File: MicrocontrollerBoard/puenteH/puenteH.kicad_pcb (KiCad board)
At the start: 2 copper layers, 78.7 x 63.5 mm, 54 parts, among them J1 PROG_CONN, J10 PCA_5V, J11 PCB_5V, J12 PDA_5V, J13 PA_GND, J14 PBA_GND, J15 PCA_GND, J16 PCB_GND, J17 PDA_GND, J18 COM, J19 COM_5V, J2 5V_CONN, J20 COM_GND, J21 POWER_CONN, J22 MOTOR2, J23 MOTOR1, J3 PA, J4 PBA, J5 PCA, J6 PCB, J7 PDA, J8 PA_5V, J9 PBA_5V, U1 ATmega1284P-PU, U2 TC4422, U3 TC4422, U4 TC4422, U5 TC4422, Y1 16MHz

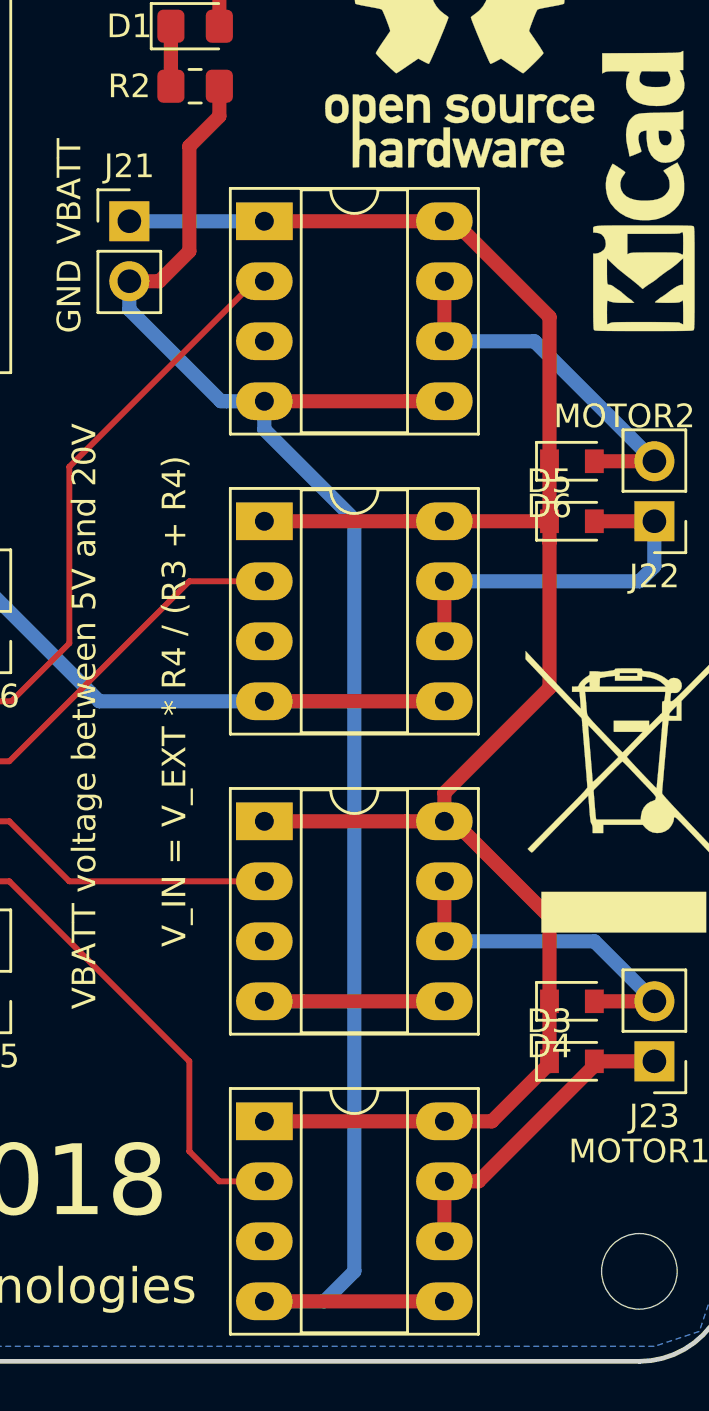
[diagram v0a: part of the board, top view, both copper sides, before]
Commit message: Changed TC4422 footprints to non socket so the 3D model has the chips.
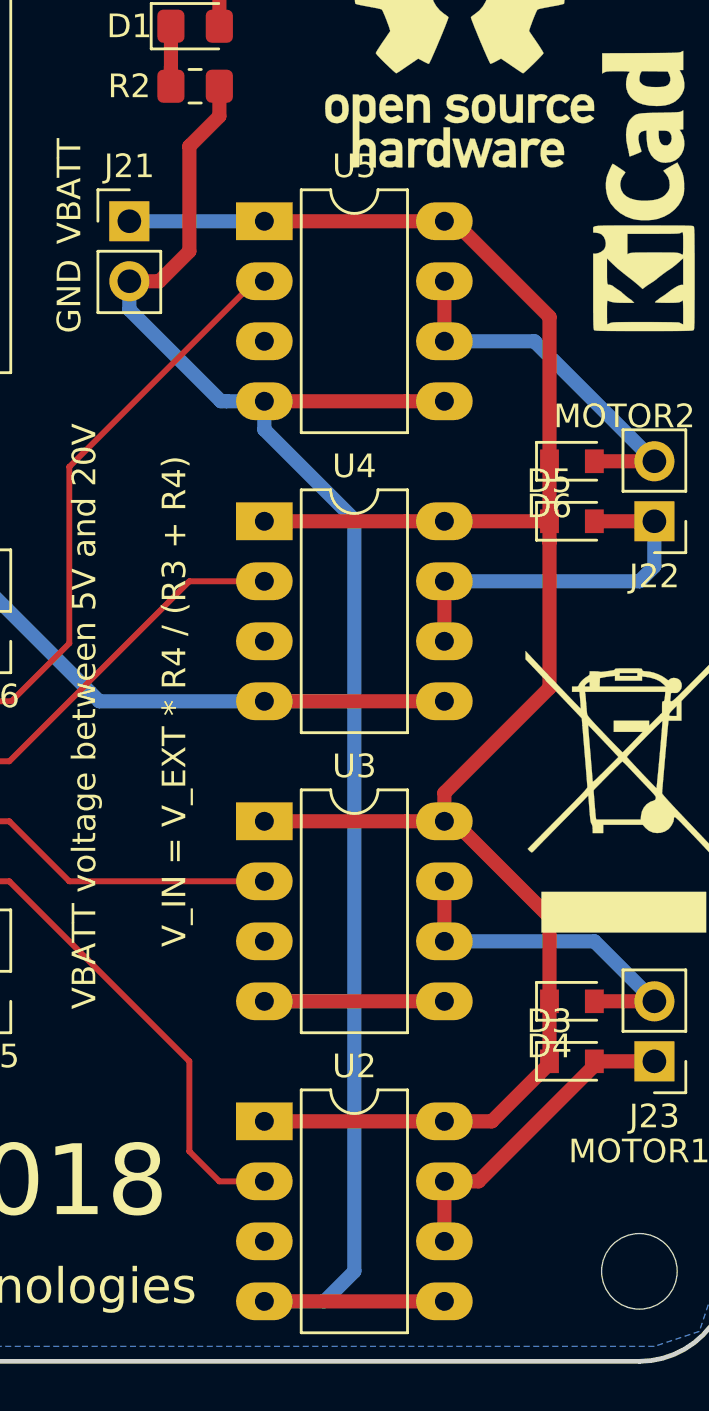
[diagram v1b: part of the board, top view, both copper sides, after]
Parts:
- U2, U3, U4, U5: footprint Package_DIP:DIP-8_W7.62mm_Socket_LongPads -> Package_DIP:DIP-8_W7.62mm_LongPads

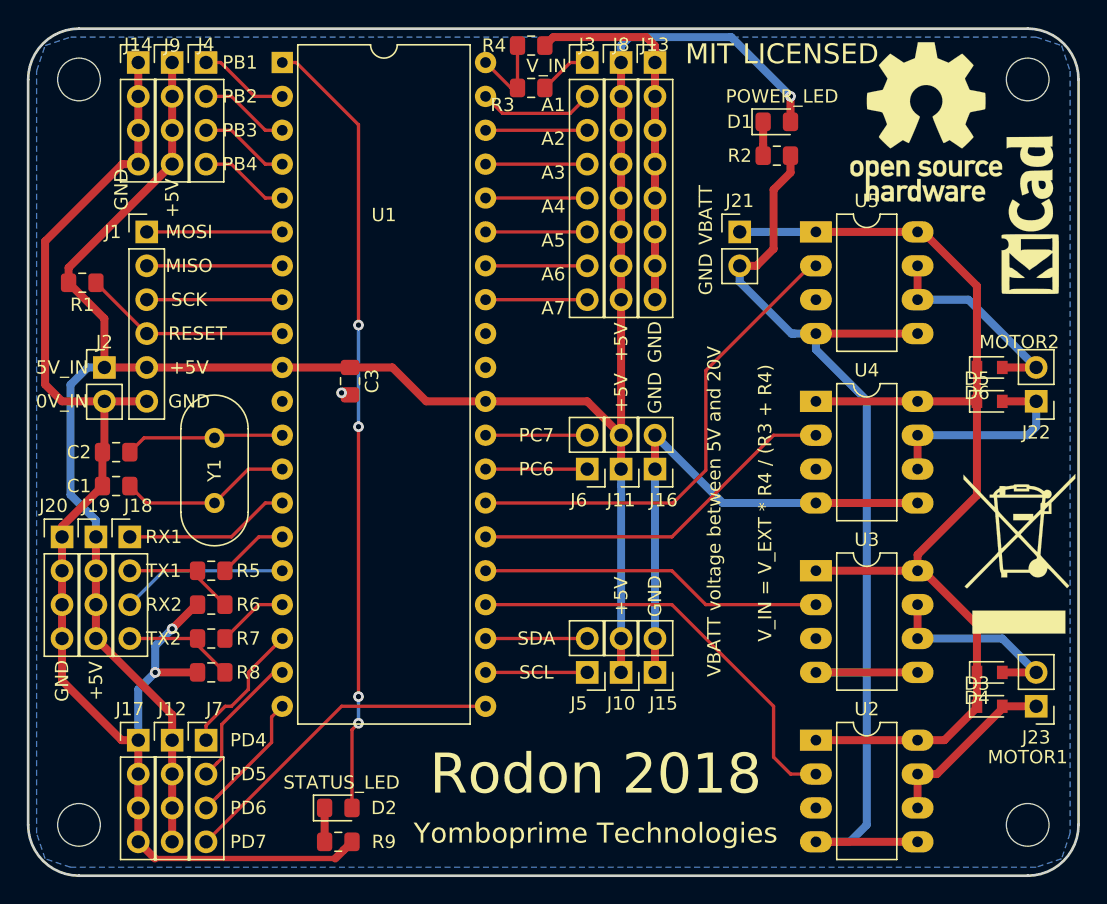
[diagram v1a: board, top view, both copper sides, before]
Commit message: Microcontroller bord: Fixed PWM lines not going to uc's PWM pins. Added 3V3 regulator.
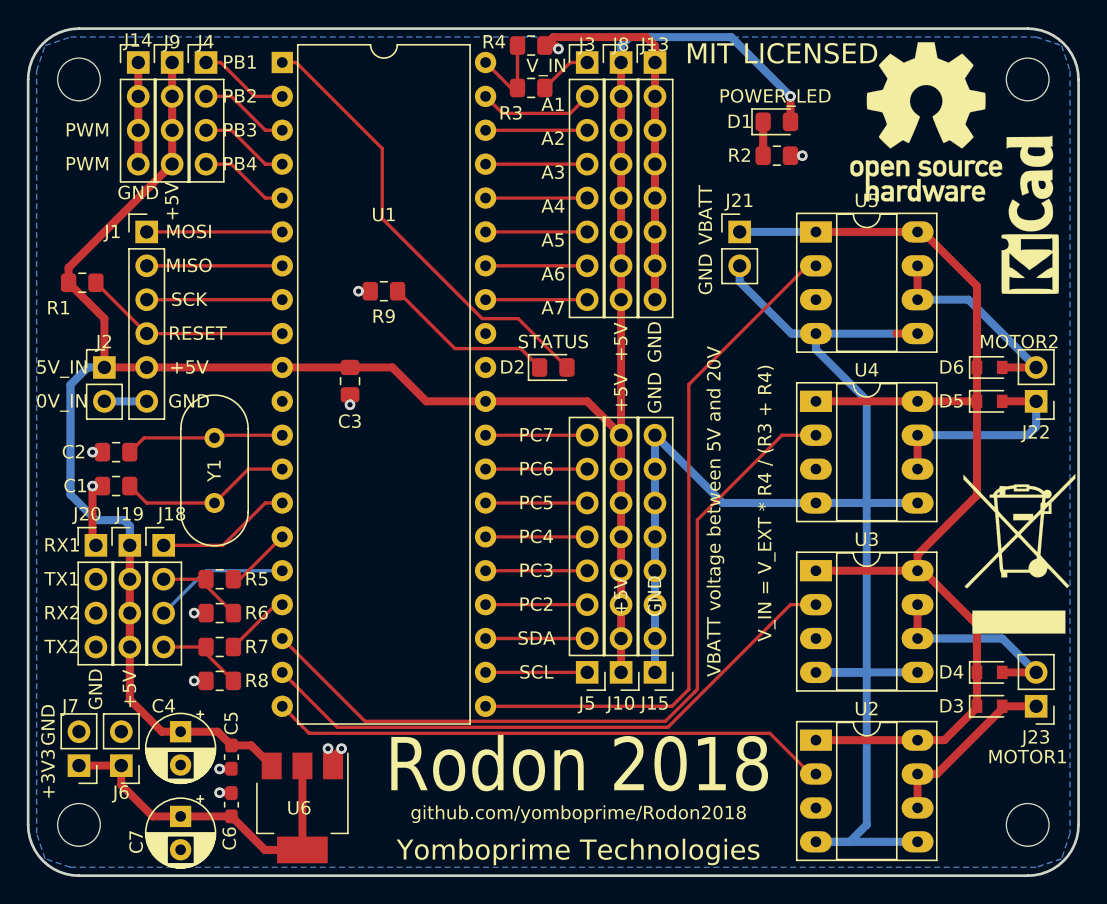
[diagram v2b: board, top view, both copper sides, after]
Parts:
- removed J11: PCB_5V, Connector_PinHeader_2.54mm:PinHeader_1x02_P2.54mm_Vertical
- removed J12: PDA_5V, Connector_PinHeader_2.54mm:PinHeader_1x04_P2.54mm_Vertical
- removed J16: PCB_GND, Connector_PinHeader_2.54mm:PinHeader_1x02_P2.54mm_Vertical
- removed J17: PDA_GND, Connector_PinHeader_2.54mm:PinHeader_1x04_P2.54mm_Vertical
- added C4: 100uF, Capacitor_THT:CP_Radial_D5.0mm_P2.50mm, F.Cu at (86.4, 103.5)
- added C5: 100nF, Capacitor_SMD:C_0603_1608Metric_Pad1.05x0.95mm_HandSolder, F.Cu at (90.2, 105.4)
- added C6: 100nF, Capacitor_SMD:C_0603_1608Metric_Pad1.05x0.95mm_HandSolder, F.Cu at (90.2, 109.0)
- added C7: 100uF, Capacitor_THT:CP_Radial_D5.0mm_P2.50mm, F.Cu at (86.4, 109.9)
- added U6: AMS1117-3.3, Package_TO_SOT_SMD:SOT-223-3_TabPin2, F.Cu at (95.5, 109.2)
- J10: value PCA_5V -> PC_5V; footprint Connector_PinHeader_2.54mm:PinHeader_1x02_P2.54mm_Vertical -> Connector_PinHeader_2.54mm:PinHeader_1x08_P2.54mm_Vertical
- J14: value PBA_GND -> PB_GND
- J15: value PCA_GND -> PC_GND; footprint Connector_PinHeader_2.54mm:PinHeader_1x02_P2.54mm_Vertical -> Connector_PinHeader_2.54mm:PinHeader_1x08_P2.54mm_Vertical
- J4: value PBA -> PB
- J5: value PCA -> PC; footprint Connector_PinHeader_2.54mm:PinHeader_1x02_P2.54mm_Vertical -> Connector_PinHeader_2.54mm:PinHeader_1x08_P2.54mm_Vertical
- J6: value PCB -> 3V_CONN_1
- J7: value PDA -> 3V_CONN_2; footprint Connector_PinHeader_2.54mm:PinHeader_1x04_P2.54mm_Vertical -> Connector_PinHeader_2.54mm:PinHeader_1x02_P2.54mm_Vertical
- J9: value PBA_5V -> PB_5V
- U2, U3, U4, U5: footprint Package_DIP:DIP-8_W7.62mm_LongPads -> Package_DIP:DIP-8_W7.62mm_Socket_LongPads
- moved R9 41.4 mm to (101.6, 70.5), turned to 0 degrees
- moved J6 41.4 mm to (81.9, 106.0)
- moved D2 36.7 mm to (114.3, 76.2)
- moved J7 9.71 mm to (78.7, 106.0), turned to 180 degrees
- moved J18 2.62 mm to (85.1, 89.5)
- moved J20 2.62 mm to (80.0, 89.5)
- moved J19 2.62 mm to (82.5, 89.5)
- moved R5 0.90 mm to (89.3, 92.1)
- moved R7 0.90 mm to (89.3, 97.2)
- moved R6 0.90 mm to (89.3, 94.6)
- moved R8 0.90 mm to (89.3, 99.7)
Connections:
- J6 pad 1: Net-(J6-Pad1) -> Net-(C6-Pad1)
- J6 pad 2: Net-(J6-Pad2) -> GND
- J7 pad 1: Net-(J7-Pad1) -> Net-(C6-Pad1)
- J7 pad 2: Net-(J7-Pad2) -> GND
- U1 pad 18: Net-(J7-Pad1) -> MOTOR2A
- U1 pad 19: Net-(J7-Pad2) -> MOTOR1B
- U1 pad 20: Net-(J7-Pad3) -> MOTOR1A
- U1 pad 21: Net-(J7-Pad4) -> MOTOR2B
- U1 pad 24: MOTOR1A -> Net-(J5-Pad3)
- U1 pad 25: MOTOR1B -> Net-(J5-Pad4)
- U1 pad 26: MOTOR2A -> Net-(J5-Pad5)
- U1 pad 27: MOTOR2B -> Net-(J5-Pad6)
- U1 pad 28: Net-(J6-Pad1) -> Net-(J5-Pad7)
- U1 pad 29: Net-(J6-Pad2) -> Net-(J5-Pad8)
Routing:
- net GND: track 265.3 -> 176.4 mm, vias 3 -> 12
- net MOTOR2A: track 27.9 -> 58.9 mm
- net Net-(C6-Pad1): track 0.00 -> 26.5 mm
- net STATUS_LED: track 59.1 -> 33.9 mm, vias 4 -> 0
- net Net-(J7-Pad4): track 25.2 -> 0.00 mm
- net MOTOR1B: track 25.8 -> 45.5 mm
- net MOTOR2B: track 36.5 -> 51.8 mm
- net Net-(D2-Pad1): track 2.54 -> 13.0 mm
- net Net-(J7-Pad2): track 10.4 -> 0.00 mm
- net Net-(J7-Pad1): track 10.3 -> 0.00 mm
- net Net-(J7-Pad3): track 9.99 -> 0.00 mm
- net MOTOR1A: track 32.3 -> 42.1 mm
- net Net-(J6-Pad2): track 7.62 -> 0.00 mm
- net Net-(J6-Pad1): track 7.62 -> 0.00 mm
- net Net-(J5-Pad8): track 0.00 -> 7.62 mm
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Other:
- board text added: "+3V3"
- board text added: "PC2"
- board text added: "PC3"
- board text added: "PC4"
- board text added: "PC5"
- board text added: "PWM"
- board text added: "STATUS"
- board text added: "github.com/yomboprime/Rodon2018"
- board text removed: "PD4"
- board text removed: "PD5"
- board text removed: "PD6"
- board text removed: "PD7"
- board text removed: "STATUS_LED"

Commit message: Microcontroller board: Some minor fixes.
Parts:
- moved REF** 1.78 mm to (149.1, 88.4)
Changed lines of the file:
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@@
   (general
     (thickness 1.6)
-    (drawings 66)
+    (drawings 64)
     (tracks 275)
     (zones 0)
@@
     (descr "8-lead though-hole mounted DIP package, row spacing 7.62 mm (300 mils), Socket, LongPads")
     (tags "THT DIP DIL PDIP 2.54mm 7.62mm 300mil Socket LongPads")
-    (fp_text reference U4 (at 3.81 -2.33) (layer F.SilkS)
+    (fp_text reference U4 (at 3.81 1.905) (layer F.SilkS)
       (effects (font (size 1 1) (thickness 0.15)))
     )
@@
     (descr "Through hole straight pin header, 1x02, 2.54mm pitch, single row")
     (tags "Through hole pin header THT 1x02 2.54mm single row")
-    (fp_text reference J23 (at 0 -2.33 180) (layer F.SilkS)
+    (fp_text reference J23 (at 0.127 4.953 180) (layer F.SilkS)
       (effects (font (size 1 1) (thickness 0.15)))
     )
@@
   )
   (module Symbol:WEEE-Logo_8.4x12mm_SilkScreen (layer F.Cu)
-    (at 149.225 90.17)
+    (at 149.098 88.392)
     (descr "Waste Electrical and Electronic Equipment Directive")
     (tags "Logo WEEE")
@@
     (descr "8-lead though-hole mounted DIP package, row spacing 7.62 mm (300 mils), Socket, LongPads")
     (tags "THT DIP DIL PDIP 2.54mm 7.62mm 300mil Socket LongPads")
-    (fp_text reference U2 (at 3.81 -2.33) (layer F.SilkS)
+    (fp_text reference U2 (at 3.81 1.27) (layer F.SilkS)
       (effects (font (size 1 1) (thickness 0.15)))
     )
@@
     (descr "8-lead though-hole mounted DIP package, row spacing 7.62 mm (300 mils), Socket, LongPads")
     (tags "THT DIP DIL PDIP 2.54mm 7.62mm 300mil Socket LongPads")
-    (fp_text reference U3 (at 3.81 -2.33) (layer F.SilkS)
+    (fp_text reference U3 (at 3.81 1.651) (layer F.SilkS)
       (effects (font (size 1 1) (thickness 0.15)))
     )
@@
     (descr "8-lead though-hole mounted DIP package, row spacing 7.62 mm (300 mils), Socket, LongPads")
     (tags "THT DIP DIL PDIP 2.54mm 7.62mm 300mil Socket LongPads")
-    (fp_text reference U5 (at 3.81 -2.33) (layer F.SilkS)
+    (fp_text reference U5 (at 3.81 1.524) (layer F.SilkS)
       (effects (font (size 1 1) (thickness 0.15)))
     )
@@
     (effects (font (size 1.5 1.5) (thickness 0.3)))
   )
-  (gr_text MOTOR2 (at 149.225 74.295) (layer F.SilkS)
+  (gr_text MOTOR2 (at 149.225 74.041) (layer F.SilkS)
     (effects (font (size 1 1) (thickness 0.15)))
   )
-  (gr_text MOTOR1 (at 149.86 105.41) (layer F.SilkS)
+  (gr_text MOTOR1 (at 149.86 104.267) (layer F.SilkS)
     (effects (font (size 1 1) (thickness 0.15)))
   )
@@
     (effects (font (size 1 1) (thickness 0.15)))
   )
-  (gr_text GND (at 121.92 93.345 90) (layer F.SilkS)
-    (effects (font (size 1 1) (thickness 0.15)))
-  )
-  (gr_text +5V (at 119.38 93.345 90) (layer F.SilkS)
-    (effects (font (size 1 1) (thickness 0.15)))
-  )
